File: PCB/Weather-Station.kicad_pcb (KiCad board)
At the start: 2 copper layers, 65 x 60 mm, 49 parts, among them J10 Conn_01x02, J11 Conn_01x02, J12 Conn_01x02, J13 Conn_01x02, J14 Conn_01x02, J15 Conn_01x02, J3 DataLogger, J4 BME280, J7 FTDI, J8 Conn_01x02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

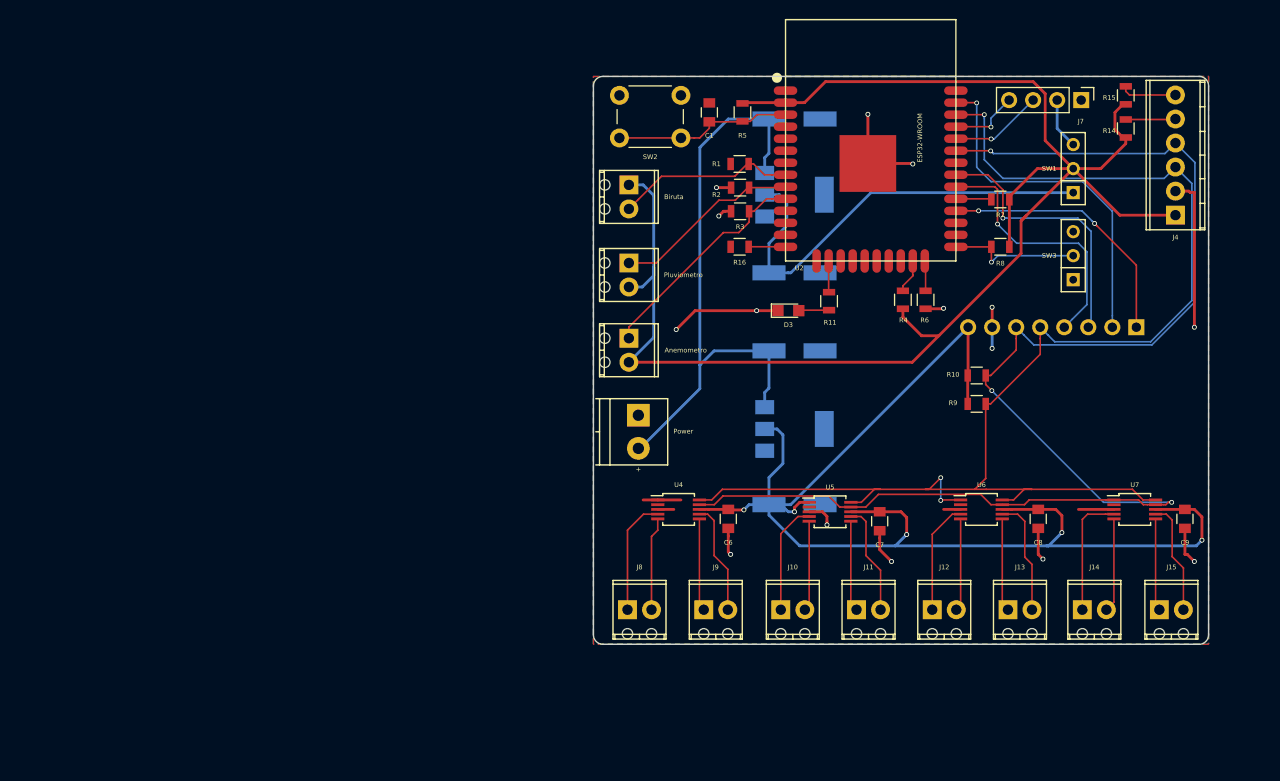
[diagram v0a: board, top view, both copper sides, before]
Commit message: Colocando mountholes e silkscreens
Signed-off-by: Gustavo Costa <gustavocosta@ic.ufal.br>
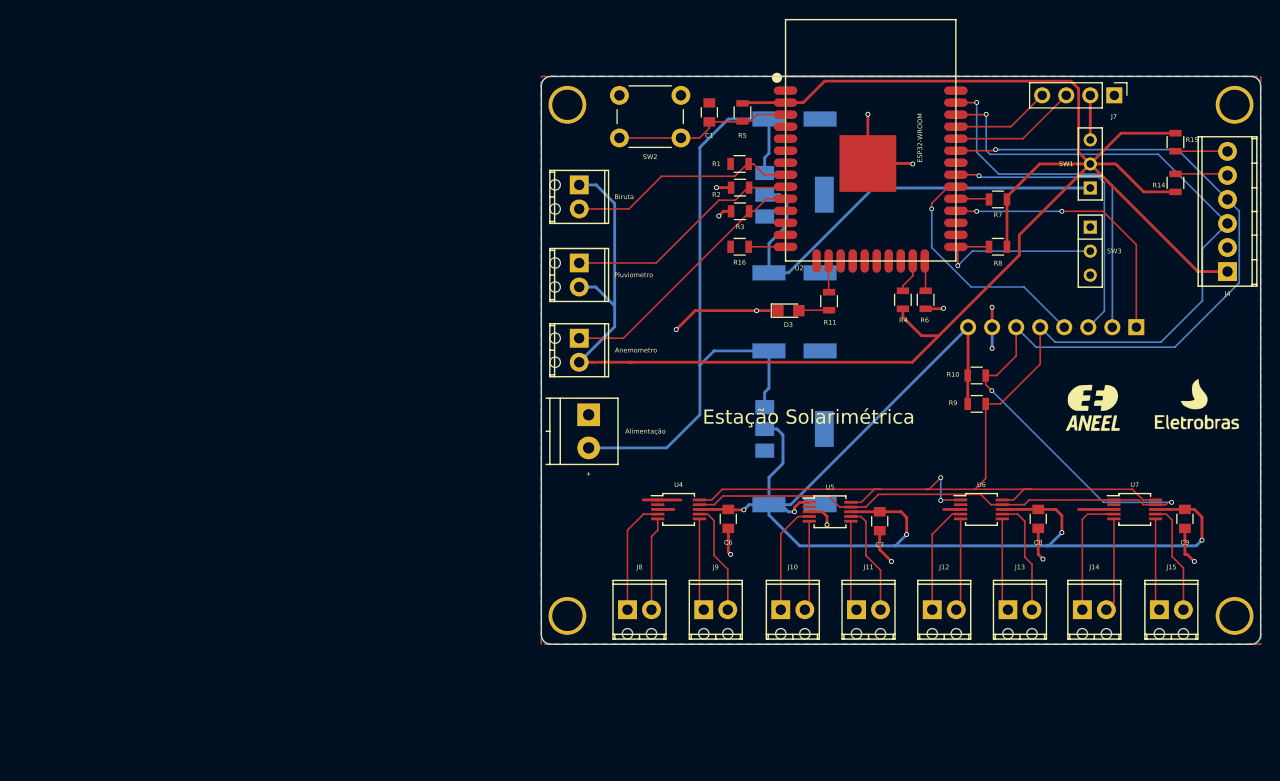
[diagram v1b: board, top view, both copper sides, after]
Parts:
- added ?: padhole, MPPT_Library:padhole, F.Cu at (119.8, 53.0)
- added ?: padhole, MPPT_Library:padhole, F.Cu at (190.2, 53.0)
- added ?: padhole, MPPT_Library:padhole, F.Cu at (119.8, 107.0)
- added ?: padhole, MPPT_Library:padhole, F.Cu at (190.2, 107.0)
- added G***: LOGO, MPPT_Library:aneel, F.Cu at (175.2, 85.0)
- added G***: LOGO, MPPT_Library:eletrobras, F.Cu at (186.2, 84.5)
- moved J4 8.11 mm to (189.5, 70.6)
- moved R14 7.79 mm to (184.0, 61.2)
- moved R15 7.22 mm to (184.0, 57.0), turned to 90 degrees
- moved Alimentação 5.25 mm to (122.0, 85.8)
- moved Anemometro 5.25 mm to (121.0, 77.7)
- moved Biruta 5.25 mm to (121.0, 61.5)
- moved Pluviometro 5.25 mm to (121.0, 69.7)
- moved J7 3.54 mm to (177.5, 52.0)
- moved SW1 1.87 mm to (175.0, 59.2)
- moved SW3 1.86 mm to (175.0, 68.5), turned to 270 degrees
- moved R7 0.25 mm to (165.2, 63.0)
- moved R8 0.25 mm to (165.2, 68.0)
- renumbered Power to Alimentação
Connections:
- SW3 pad 1: Net-(SW3-Pad1) -> (no net)
- U2 pad 11: Net-(U2-Pad11) -> (no net)
- U2 pad 12: Net-(U2-Pad12) -> (no net)
- U2 pad 13: Net-(U2-Pad13) -> (no net)
- U2 pad 17: Net-(U2-Pad17) -> (no net)
- U2 pad 18: Net-(U2-Pad18) -> (no net)
- U2 pad 19: Net-(U2-Pad19) -> (no net)
- U2 pad 20: Net-(U2-Pad20) -> (no net)
- U2 pad 21: Net-(U2-Pad21) -> (no net)
- U2 pad 22: Net-(U2-Pad22) -> (no net)
- U2 pad 26: Net-(U2-Pad26) -> (no net)
- U2 pad 27: Net-(U2-Pad27) -> (no net)
- U2 pad 32: Net-(U2-Pad32) -> (no net)
- U2 pad 4: Net-(U2-Pad4) -> (no net)
- U2 pad 5: Net-(U2-Pad5) -> (no net)
- U2 pad 6: Net-(U2-Pad6) -> (no net)
- U2 pad 7: Net-(U2-Pad7) -> (no net)
- U4 pad 2: Net-(U4-Pad2) -> (no net)
- U5 pad 2: Net-(U5-Pad2) -> (no net)
- U6 pad 2: Net-(U6-Pad2) -> (no net)
- U7 pad 2: Net-(U7-Pad2) -> (no net)
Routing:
- net +3V3: track 170.1 -> 197.9 mm
- net GND: track 75.5 -> 59.2 mm, vias 15 -> 14
- net Net-(C2-Pad1): track 63.1 -> 69.9 mm
- net Net-(R8-Pad1): track 14.6 -> 20.2 mm
- net Net-(J5-Pad1): track 19.9 -> 25.1 mm
- net Net-(J1-Pad2): track 19.0 -> 24.2 mm
- net SDA: track 147.7 -> 152.7 mm
- net Net-(J6-Pad1): track 24.0 -> 28.0 mm
- net RXD: track 9.87 -> 13.6 mm, vias 1 -> 0
- net MISO: track 28.8 -> 32.4 mm
- net TXD: track 7.36 -> 10.5 mm, vias 1 -> 0
- net SCL: track 145.9 -> 148.5 mm
- net SCK: track 27.8 -> 25.4 mm
- net Net-(C3-Pad1): track 46.6 -> 48.6 mm
- net CS: track 28.0 -> 29.3 mm
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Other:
- board size 65 x 60 mm -> 76 x 60 mm
- board text added: "Estação Solarimétrica"

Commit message: Fazendo PCB com o data logger
Signed-off-by: Gustavo Costa <gustavocosta@ic.ufal.br>
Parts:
- added BT1: Battery_Cell, Battery_Holders:Keystone_3000_1x12mm-CoinCell, B.Cu at (185.0, 83.2)
- added R12: 10k, Resistors_SMD:R_0805, F.Cu at (171.0, 88.5)
- added U8: 74HC125D, Housings_SOIC:SOIC-14_3.9x8.7mm_Pitch1.27mm, F.Cu at (165.0, 84.8)
- added U9: DS13072, Housings_SOIC:SOIC-8_3.9x4.9mm_Pitch1.27mm, B.Cu at (169.8, 82.8)
- added Y1: Crystal, Crystals:Crystal_DS15_d1.5mm_l5.0mm_Horizontal, B.Cu at (158.8, 85.0)
- J3: value DataLogger -> Micro_SD_Card; footprint Pin_Headers:Pin_Header_Straight_1x08_Pitch2.54mm -> MPPT_Library:Conn_uSDcard; moved to F.Cu
- R14, R15: moved to B.Cu
- moved G*** 108.1 mm to (73.0, 120.0)
- moved G*** 106.4 mm to (85.8, 119.5)
- moved R10 29.0 mm to (189.0, 94.5), turned to 180 degrees
- moved R9 27.1 mm to (189.0, 92.2), turned to 180 degrees
- moved R15 13.8 mm to (184.2, 70.8), turned to 180 degrees
- moved J3 9.81 mm to (187.8, 82.3)
- moved R14 6.75 mm to (184.2, 68.0), turned to 180 degrees
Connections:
- J3 pad 1: CS -> (no net)
- J3 pad 2: MOSI -> Net-(J3-Pad2)
- J3 pad 3: MISO -> Net-(J3-Pad3)
- J3 pad 4: SCK -> +3V3
- J3 pad 5: SCL -> Net-(J3-Pad5)
- J3 pad 6: SDA -> GND
- J3 pad 7: GND -> MISO
- J3 pad 8: +5V -> (no net)
- J4 pad 1: +3V3 -> Net-(J4-Pad1)
- J4 pad 2: GND -> Net-(J4-Pad2)
- J4 pad 3: SCL -> SDA
- J4 pad 4: SDA -> SCL
- J4 pad 5: Net-(J4-Pad5) -> GND
- J4 pad 6: Net-(J4-Pad6) -> +3V3
- R14 pad 1: Net-(J4-Pad5) -> Net-(J4-Pad2)
- R15 pad 1: Net-(J4-Pad6) -> Net-(J4-Pad1)
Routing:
- net +3V3: track 197.9 -> 234.0 mm, vias 0 -> 1
- net SDA: track 152.7 -> 121.1 mm, vias 3 -> 0
- net Net-(J3-Pad5): track 0.00 -> 30.7 mm
- net MISO: track 32.4 -> 2.48 mm
- net Net-(J3-Pad3): track 0.00 -> 23.4 mm
- net Net-(BT1-Pad1): track 0.00 -> 20.8 mm
- net Net-(J3-Pad2): track 0.00 -> 15.2 mm
- net CS: track 29.3 -> 40.9 mm
- net Net-(U9-Pad1): track 0.00 -> 8.42 mm
- net Net-(U9-Pad2): track 0.00 -> 8.36 mm
- net SCL: track 148.5 -> 142.2 mm, vias 3 -> 2
- net Net-(J4-Pad5): track 5.57 -> 0.00 mm
- net Net-(J4-Pad6): track 5.51 -> 0.00 mm
- net +5V: track 136.3 -> 141.5 mm, vias 5 -> 6
- net Net-(J4-Pad1): track 0.00 -> 4.35 mm
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
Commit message: Finalizando PCB
Signed-off-by: Gustavo Costa <gustavocosta@ic.ufal.br>
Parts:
- moved G*** 71.4 mm to (136.5, 87.2)
- moved G*** 70.8 mm to (148.8, 87.2)
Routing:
- net MISO: track 2.48 -> 61.0 mm, vias 1 -> 3
- net SDA: track 121.1 -> 140.9 mm, vias 0 -> 1
- net GND: track 54.9 -> 72.2 mm, vias 12 -> 17
- net SCL: track 142.2 -> 154.9 mm, vias 2 -> 3
- net +5V: track 141.5 -> 149.5 mm
